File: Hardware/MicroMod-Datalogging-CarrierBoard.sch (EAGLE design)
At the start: 64 parts, among them J11 microSD, J12 SPI, J14 I2C, J2 JTAG, J3 QWIIC_RIGHT_ANGLE, J5 UART, J6 MICROMOD-2222-C, J8 Dedicated, Q2 20V/4.2A/52mΩ/1.4W, Q4 20V/4.2A/52mΩ/1.4W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

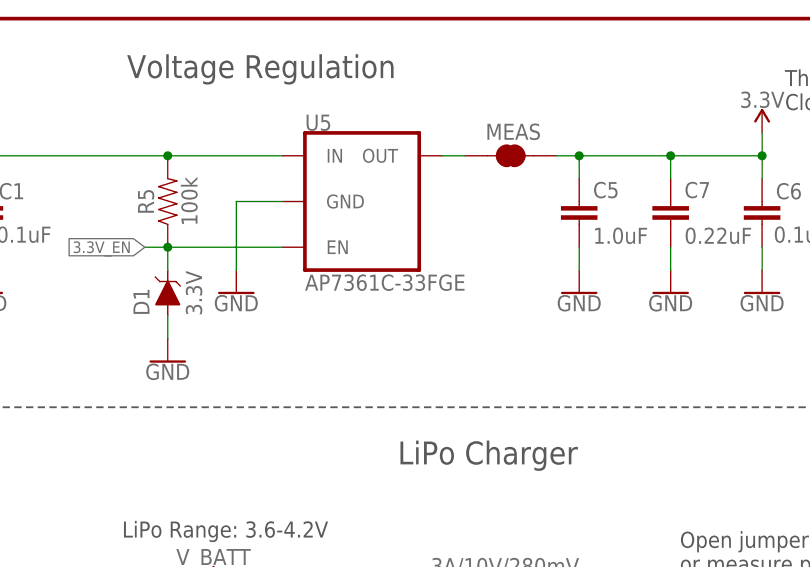
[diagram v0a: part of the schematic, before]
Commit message: Update v-reg device
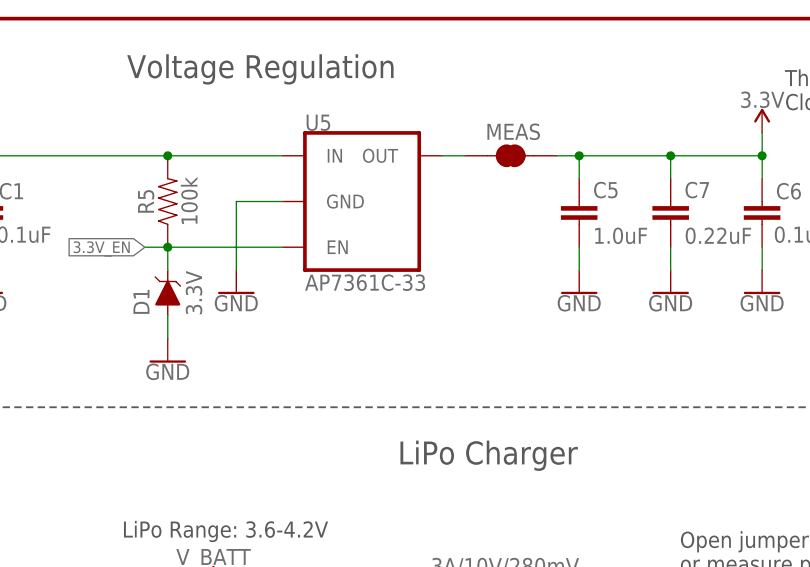
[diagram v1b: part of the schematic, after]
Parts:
- U5: value AP7361C-33FGE -> AP7361C-33; device ublox:AP7361C-33FGE -> SparkFun-IC-Power:AP7361C-33FGEUDFN-8
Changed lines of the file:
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@@
 <part name="GND10" library="SparkFun-PowerSymbols" deviceset="GND" device=""/>
 <part name="SUPPLY5" library="SparkFun-PowerSymbols" deviceset="V_USB" device=""/>
-<part name="U5" library="ublox" deviceset="AP7361C-33FGE" device=""/>
+<part name="U5" library="SparkFun-IC-Power" deviceset="AP7361C-33FGE" device="UDFN-8" value="AP7361C-33"/>
 <part name="GND20" library="SparkFun-PowerSymbols" deviceset="GND" device=""/>
 <part name="C13" library="SparkFun-Capacitors" deviceset="0.22UF" device="-0603-25V-10%" value="0.22uF"/>

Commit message: Change peripheral power to regulators. Upgrade buzzard labels. Add VE jumper.
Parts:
- removed Q2, Q4: 20V/4.2A/52mΩ/1.4W, SparkFun-DiscreteSemi:MOSFET_PCH-DMG2305UX-7
- added 3V3_LED, VIN_LED: JUMPER-SMT_2_NC_TRACE_SILK, SparkFun-Jumpers:JUMPER-SMT_2_NC_TRACE_SILK
- added D4: BAS70-05, SparkFun-DiscreteSemi:DIODE-SCHOTTKY-DUAL
- added D5: RED, SparkFun-LED:LED-RED0603
- added J13: (no value), SparkFun-Connectors:CONN_01PTH_NO_SILK_YES_STOP
- added R11: 1k, SparkFun-Resistors:1KOHM-0603-1/10W-1%
- added R12: 4.7k, SparkFun-Resistors:4.7KOHM-0603-1/10W-1%
- added R13, R14, R15: 100k, SparkFun-Resistors:100KOHM-0603-1/10W-1%
- added U1, U3: 3.3V, SparkFun-IC-Power:V_REG_AP2112K-3.3V
- added VE: JUMPER-SMT_2_NO_SILK, SparkFun-Jumpers:JUMPER-SMT_2_NO_SILK
- C8: value 10uF -> 1.0uF; device SparkFun-Capacitors:10UF-0603-6.3V-20% -> SparkFun-Capacitors:1.0UF-0603-16V-10%
- D7: value 1A/23V/620mV -> Yellow; device SparkFun-DiscreteSemi:DIODE-SCHOTTKY-BAT20J -> SparkFun-LED:LED-YELLOW0603
- R8: value 1k -> 3.3k; device SparkFun-Resistors:1KOHM-0603-1/10W-1% -> SparkFun-Resistors:3.3KOHM-0603-1/10W-1%
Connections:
- removed net PERIPHERAL_PWR: Q2.G
- removed net SPI_MISO: J11.DAT0/MISO, J12.4, J6.SPI_MISO/SDIO_DATA0
- removed net SPI_MOSI: J11.CMD/MOSI, J12.3, J6.SPI_MOSI/SDIO_CMD
- new net 3.3V_EN_VE: D1.C, R5.1, U5.EN, VE.2
- new net N$5: D5.A, R11.1
- new net N$6: 3V3_LED.1, R11.2
- new net N$8: R12.2, VIN_LED.1
- new net N$9: D7.A, R12.1
- new net PERIPHERAL_PWR_CTRL: J6.G1/BUS1, R14.1, U3.EN
- new net SPI_CIPO: J11.DAT0/SDO, J12.4, J6.SPI_SDI/SDIO_DATA0
- new net SPI_COPI: J11.CMD/SDI, J12.3, J6.SPI_SDO/SDIO_CMD
- net !RESET!: now also J13.1
- net 3.3V: now also 3V3_LED.2, D4.A1, R13.2, R14.2; no longer C8.1, C9.1, D7.A, Q2.S, Q4.S
- net 3.3V_EN: now also VE.1; no longer D1.C, R5.1, U5.EN
- net 3.3V_LP: now also C8.1, R15.2, U3.OUT; no longer J14.2, Q2.D
- net GND: now also D5.C, D7.C, U1.GND, U3.GND
- net QWIIC_PWR: now also C9.1, J14.2, U1.OUT; no longer Q4.D
- net QWIIC_PWR_CTRL: now also J6.G2/BUS2, R13.1, U1.EN; no longer Q4.G
- net RTC_3V: now also D4.C; no longer D7.C
- net SD_!CS!: now also J11.DAT3/!CS!, R15.1; no longer J11.DAT3/CS
- net VIN: now also U1.IN, U3.IN, VIN_LED.2
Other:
- note added: "0.100uA Leakage 0.410V drop at 1mA 1.0V drop at 15mA"
- note added: "Close VE to enable processor control of 3.3V bus."
- note added: "Closing jumper bypasses PTC to allow >2A current flows."
- note added: "N. Seidle"
- note added: "SWO"
- note added: "VIN: 3.7-6.0V"
- note added: "v11"
- note removed: "0.65uA Leakage 0.3V drop at 10mA"
- note removed: "JTAG"
- note removed: "This is the penny-in-the-fuse jumper. Close only if you know what you're doing."
- moved on the sheet: BT1, BYP, C1, C13, C2, C3, C4, C46, C5, C6, C7, C8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

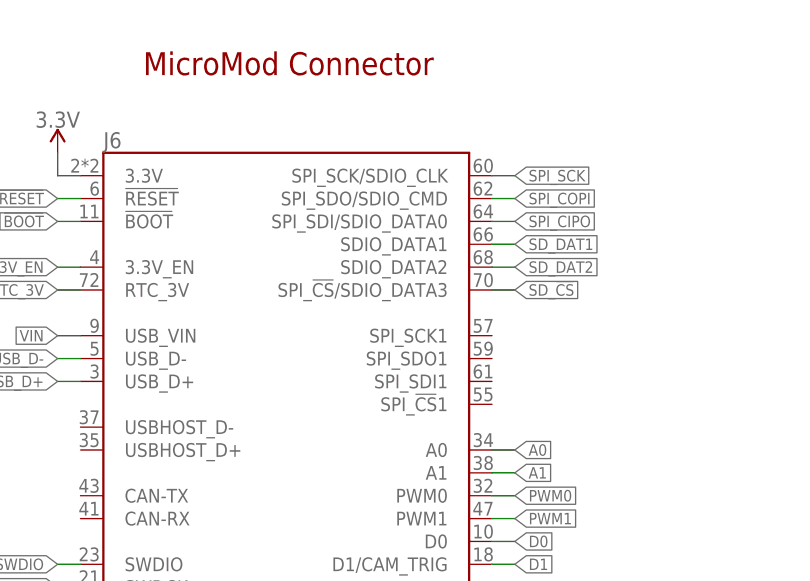
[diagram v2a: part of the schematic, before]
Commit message: Update MicroMod connector with new SPI port assignments.
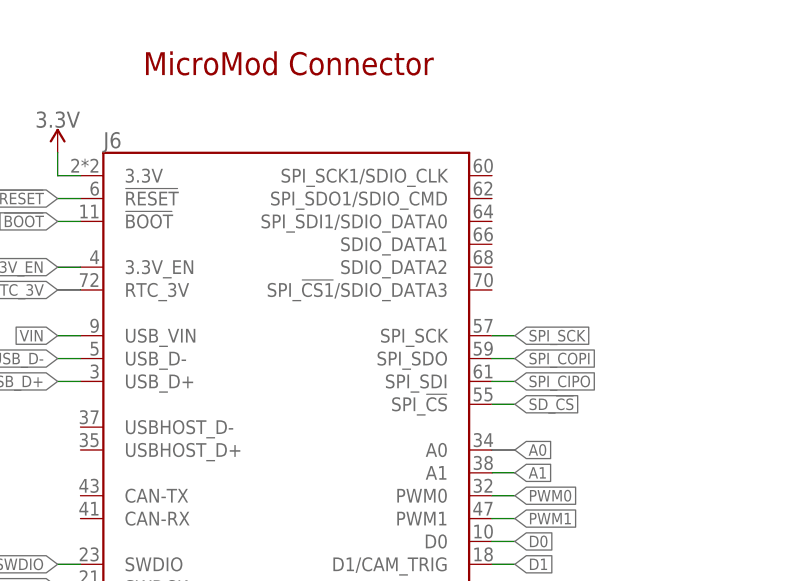
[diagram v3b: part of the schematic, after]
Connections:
- net SD_!CS!: now also J6.SPI_!CS!; no longer J6.SPI_!CS!/SDIO_DATA3
- net SD_DAT1: no longer J6.SDIO_DATA1
- net SD_DAT2: no longer J6.SDIO_DATA2
- net SPI_CIPO: now also J6.SPI_SDI; no longer J6.SPI_SDI/SDIO_DATA0
- net SPI_COPI: now also J6.SPI_SDO; no longer J6.SPI_SDO/SDIO_CMD
- net SPI_SCK: now also J6.SPI_SCK; no longer J6.SPI_SCK/SDIO_CLK
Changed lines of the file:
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@@
 <pinref part="J11" gate="G$1" pin="DAT1/NC"/>
-</segment>
-<segment>
-<wire x1="78.74" y1="116.84" x2="81.28" y2="116.84" width="0.1524" layer="91"/>
-<label x="81.28" y="116.84" size="1.27" layer="95" xref="yes"/>
-<pinref part="J6" gate="J1" pin="SDIO_DATA1"/>
 </segment>
 </net>
@@
 </segment>
 <segment>
-<wire x1="78.74" y1="124.46" x2="81.28" y2="124.46" width="0.1524" layer="91"/>
-<label x="81.28" y="124.46" size="1.27" layer="95" xref="yes"/>
-<pinref part="J6" gate="J1" pin="SPI_SCK/SDIO_CLK"/>
-</segment>
-<segment>
 <wire x1="246.38" y1="33.02" x2="243.84" y2="33.02" width="0.1524" layer="91"/>
 <label x="243.84" y="33.02" size="1.27" layer="95" rot="R180" xref="yes"/>
 <pinref part="J12" gate="G$1" pin="2"/>
+</segment>
+<segment>
+<pinref part="J6" gate="J1" pin="SPI_SCK"/>
+<wire x1="78.74" y1="106.68" x2="81.28" y2="106.68" width="0.1524" layer="91"/>
+<label x="81.28" y="106.68" size="1.27" layer="95" xref="yes"/>
 </segment>
 </net>
@@
 </segment>
 <segment>
-<wire x1="78.74" y1="111.76" x2="81.28" y2="111.76" width="0.1524" layer="91"/>
-<label x="81.28" y="111.76" size="1.27" layer="95" xref="yes"/>
-<pinref part="J6" gate="J1" pin="SPI_!CS!/SDIO_DATA3"/>
+<pinref part="J6" gate="J1" pin="SPI_!CS!"/>
+<wire x1="78.74" y1="99.06" x2="81.28" y2="99.06" width="0.1524" layer="91"/>
+<label x="81.28" y="99.06" size="1.27" layer="95" xref="yes"/>
 </segment>
 </net>
@@
 <label x="259.08" y="251.46" size="1.27" layer="95" rot="R180" xref="yes"/>
 <pinref part="J11" gate="G$1" pin="DAT2/NC"/>
-</segment>
-<segment>
-<wire x1="78.74" y1="114.3" x2="81.28" y2="114.3" width="0.1524" layer="91"/>
-<label x="81.28" y="114.3" size="1.27" layer="95" xref="yes"/>
-<pinref part="J6" gate="J1" pin="SDIO_DATA2"/>
 </segment>
 </net>
@@
 </segment>
 <segment>
-<wire x1="78.74" y1="121.92" x2="81.28" y2="121.92" width="0.1524" layer="91"/>
-<label x="81.28" y="121.92" size="1.27" layer="95" xref="yes"/>
-<pinref part="J6" gate="J1" pin="SPI_SDO/SDIO_CMD"/>
+<pinref part="J6" gate="J1" pin="SPI_SDO"/>
+<wire x1="78.74" y1="104.14" x2="81.28" y2="104.14" width="0.1524" layer="91"/>
+<label x="81.28" y="104.14" size="1.27" layer="95" xref="yes"/>
 </segment>
 </net>
@@
 </segment>
 <segment>
-<wire x1="78.74" y1="119.38" x2="81.28" y2="119.38" width="0.1524" layer="91"/>
-<label x="81.28" y="119.38" size="1.27" layer="95" xref="yes"/>
-<pinref part="J6" gate="J1" pin="SPI_SDI/SDIO_DATA0"/>
-</segment>
-</net>
+<pinref part="J6" gate="J1" pin="SPI_SDI"/>
+<wire x1="78.74" y1="101.6" x2="81.28" y2="101.6" width="0.1524" layer="91"/>
+<label x="81.28" y="101.6" size="1.27" layer="95" xref="yes"/>
+</segment>
+</net>
